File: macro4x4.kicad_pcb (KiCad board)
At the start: 2 copper layers, 100 x 100 mm, 38 parts, among them SW1 SW_Push, SW10 SW_Push, SW11 SW_Push, SW12 SW_Push, SW13 SW_Push, SW14 SW_Push, SW15 SW_Push, SW16 SW_Push, SW2 SW_Push, SW3 SW_Push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

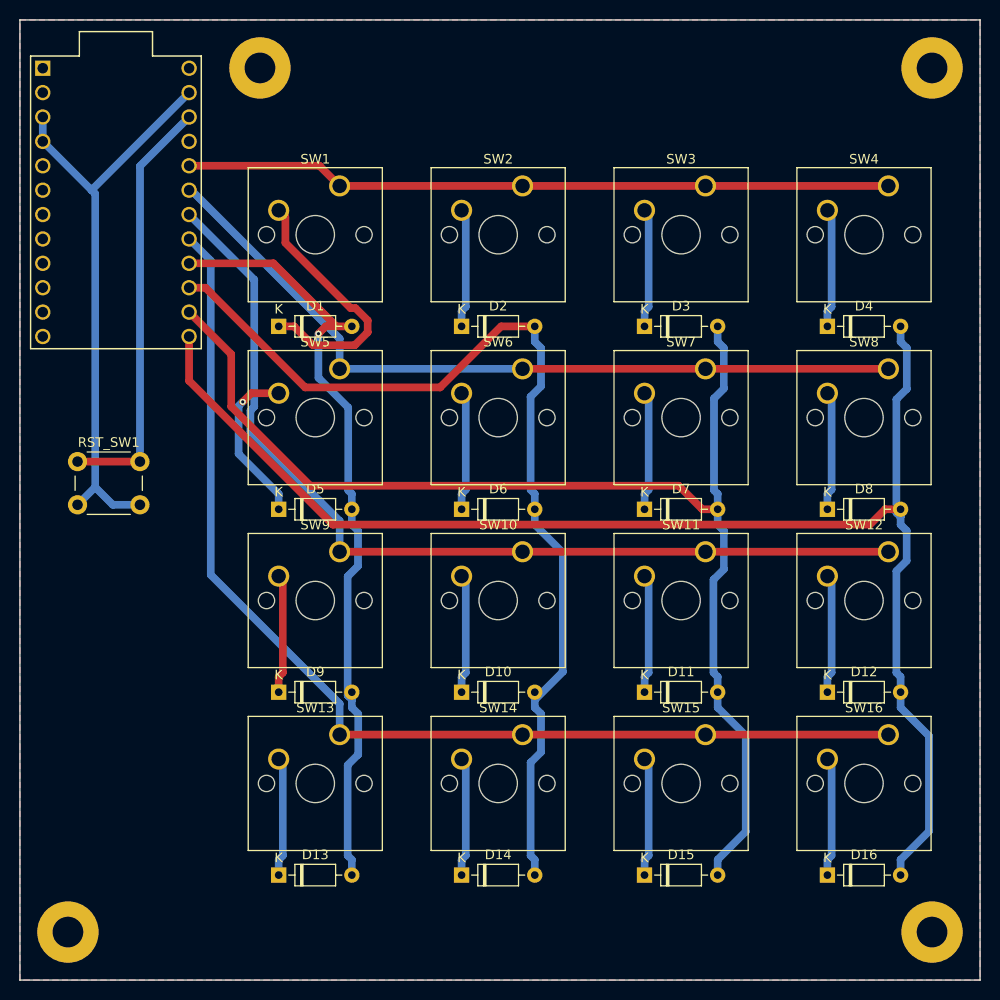
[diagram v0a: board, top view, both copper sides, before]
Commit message: ・回路図を修正 ・基板でビアを使用しないように修正
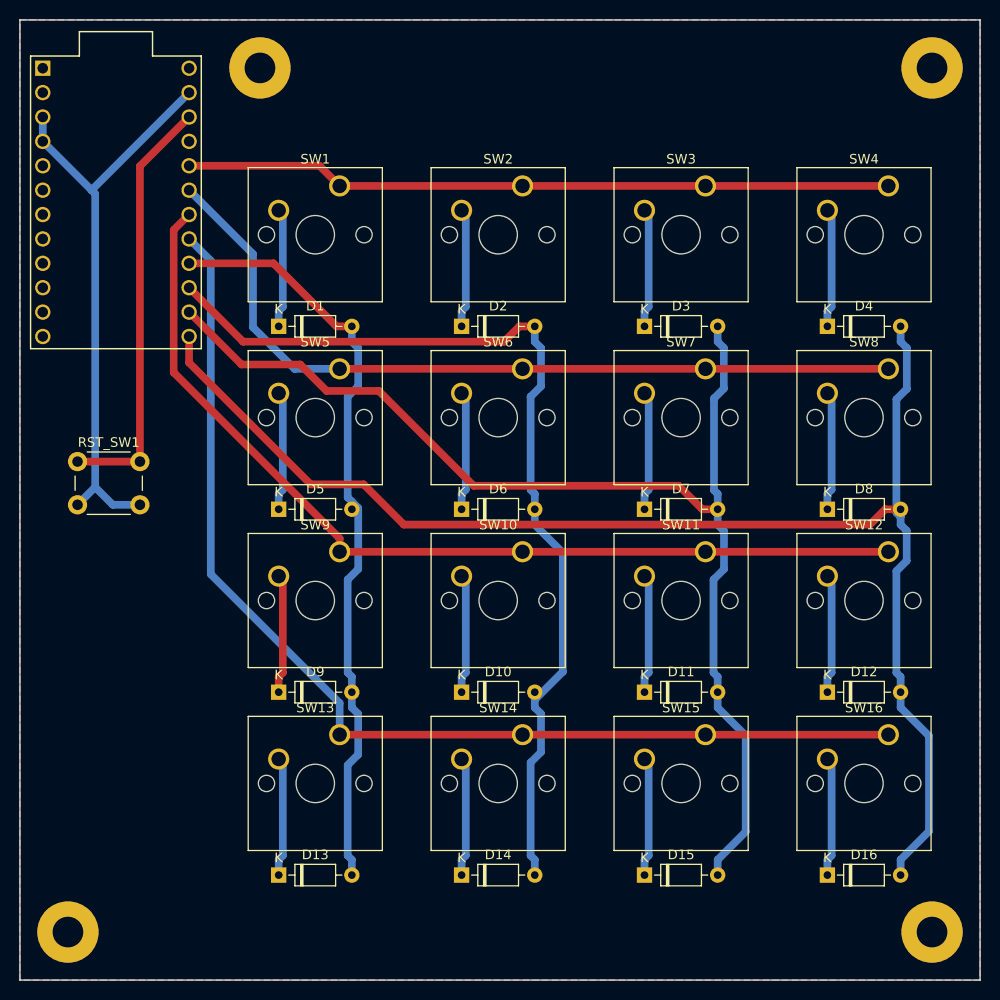
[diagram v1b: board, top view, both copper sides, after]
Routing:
- net Net-(D1-Pad1): track 27.5 -> 12.4 mm
- net Net-(D5-Pad1): track 17.2 -> 12.4 mm, vias 1 -> 0
- net COL1: track 105.1 -> 101.2 mm
- net COL2: track 128.1 -> 124.9 mm
- net ROW1: track 82.4 -> 85.0 mm
- net COL0: track 82.3 -> 80.3 mm, vias 1 -> 0
- net COL3: track 147.8 -> 146.7 mm
- net ROW2: track 99.1 -> 100.1 mm
